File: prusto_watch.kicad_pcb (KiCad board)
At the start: 2 copper layers, 42.2 x 40.9 mm, 55 parts, among them J1 USB_microB_2040002-1, J2 Conn_02x05_Odd_Even, J3 Vibration Motor, J4 Conn_01x06, J5 Conn_01x08, J6 Conn_02x03_Odd_Even, Q3 RUM002N02T2L, SW2 SW_Push, U1 STM32F303RCT6-48, U2 LTC4063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

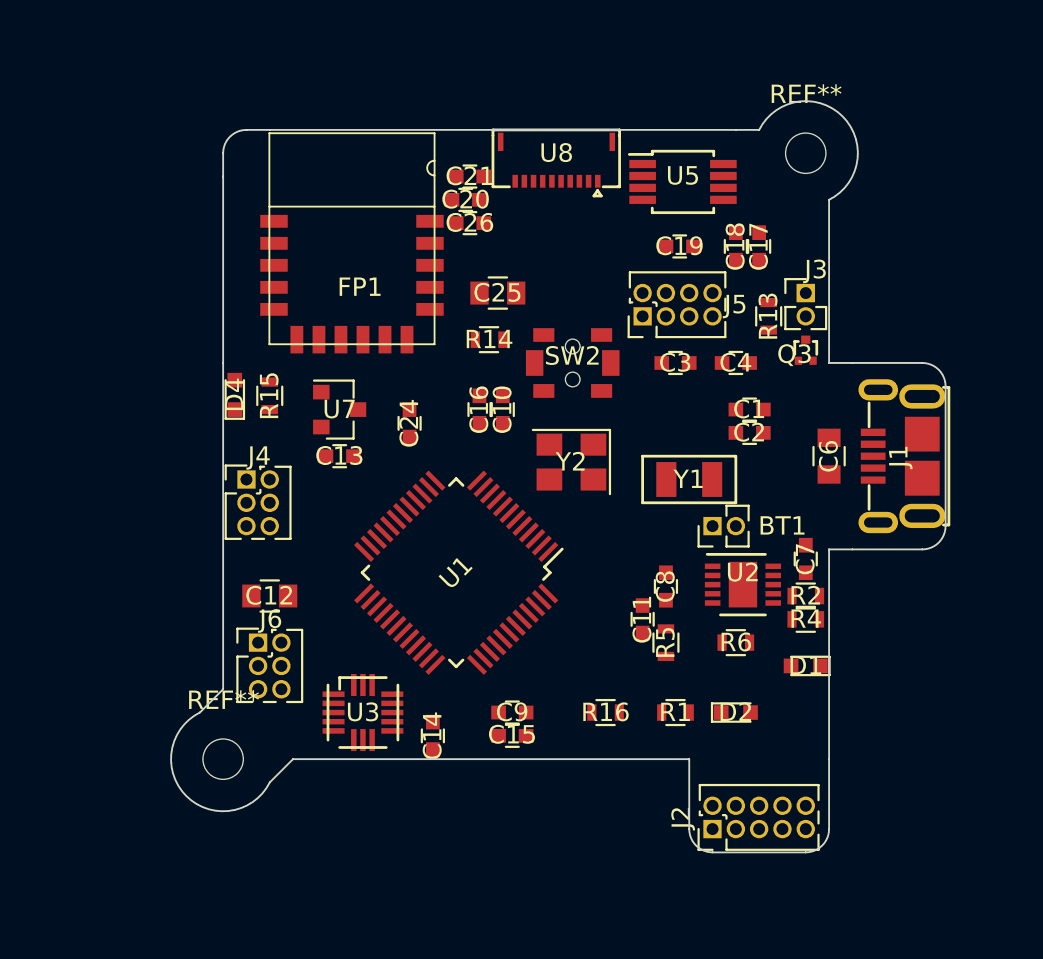
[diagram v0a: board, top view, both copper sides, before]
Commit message: Modify for better positioning
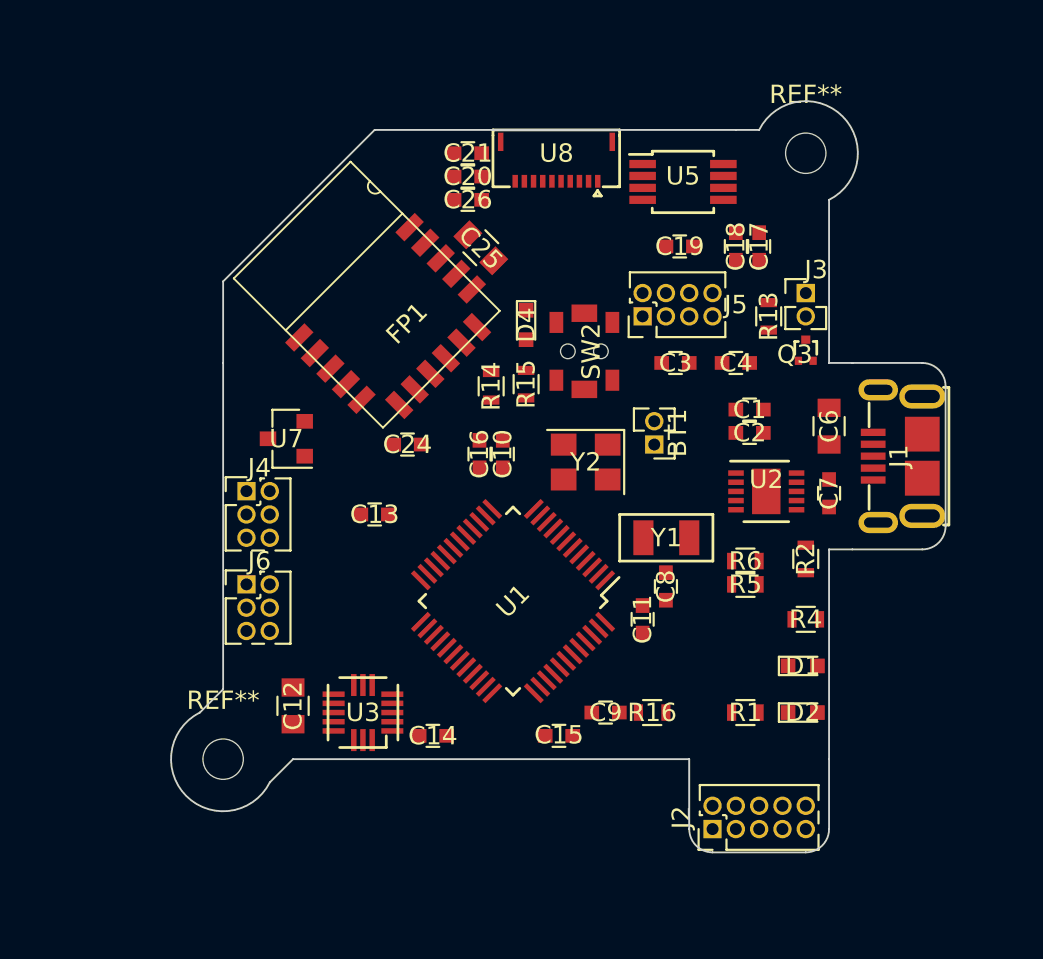
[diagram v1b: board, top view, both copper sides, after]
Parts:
- moved D4 16.3 mm to (146.1, 91.9), turned to 270 degrees
- moved R15 14.0 mm to (146.1, 95.1)
- moved FP1 7.68 mm to (138.3, 97.5), turned to 45 degrees
- moved C12 6.12 mm to (133.3, 112.7), turned to 90 degrees
- moved BT1 5.46 mm to (153.0, 98.4), turned to 180 degrees
- moved R5 5.37 mm to (158.0, 106.0), turned to 180 degrees
- moved U2 5.24 mm to (159.1, 101.0)
- moved C9 5.08 mm to (150.4, 113.0)
- moved R6 4.48 mm to (158.0, 104.8)
- moved R1 3.81 mm to (158.0, 113.0)
- moved C7 3.80 mm to (162.6, 101.1)
- moved C13 3.70 mm to (137.8, 102.2)
- moved D2 3.65 mm to (161.1, 113.0)
- moved U1 3.46 mm to (145.3, 107.0)
- moved Y1 3.41 mm to (153.7, 103.5)
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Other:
- outline, holes or cut-outs redrawn

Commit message: Rework placement
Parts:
- removed REF** (x2): MountingHole_2.2mm_M2, Mounting_Holes:MountingHole_2.2mm_M2
- added J7: Conn_02x03_Counter_Clockwise, Pin_Headers:Pin_Header_Straight_2x03_Pitch1.27mm, F.Cu at (133.3, 111.8)
- added J8: Screw_Terminal_01x01, Mounting_Holes:MountingHole_2.2mm_M2, F.Cu at (127.0, 114.9)
- added J9: Screw_Terminal_01x01, Mounting_Holes:MountingHole_2.2mm_M2, F.Cu at (164.5, 82.5)
- added R3: 10K, Resistors_SMD:R_0603, F.Cu at (138.3, 116.8)
- added R7: 10K, Resistors_SMD:R_0603, F.Cu at (133.9, 116.8)
- added R8: 10K, Resistors_SMD:R_0603, F.Cu at (142.1, 116.8)
- moved J1 39.0 mm to (128.9, 94.6), turned to 270 degrees
- moved J2 36.4 mm to (123.8, 102.9), turned to 0 degrees
- moved D1 29.8 mm to (131.4, 107.5), turned to 270 degrees
- moved C6 29.7 mm to (133.3, 91.8)
- moved J4 29.7 mm to (158.8, 111.1), turned to 180 degrees
- moved C7 28.8 mm to (135.3, 92.0), turned to 90 degrees
- moved R4 27.9 mm to (133.3, 107.4), turned to 90 degrees
- moved C12 26.8 mm to (141.0, 87.0), turned to 0 degrees
- moved R2 26.3 mm to (136.5, 95.9), turned to 0 degrees
- moved C14 24.7 mm to (142.9, 89.7), turned to 270 degrees
- moved R5 24.0 mm to (134.1, 104.1), turned to 0 degrees
- moved R16 23.8 mm to (129.5, 108.7), turned to 90 degrees
- moved U2 23.3 mm to (135.9, 99.1), turned to 90 degrees
- moved U3 23.0 mm to (139.4, 90.2), turned to 0 degrees
- moved BT1 22.5 mm to (130.8, 101.6)
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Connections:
- J1 pad 2: (no net) -> /USB_N
- J1 pad 3: (no net) -> /USB_P
- U1 pad 21: /RX_BLE -> (no net)
- U1 pad 22: /TX_BLE -> (no net)
- U1 pad 32: (no net) -> /USB_N
- U1 pad 33: (no net) -> /USB_P
- U1 pad 42: (no net) -> /RX_BLE
- U1 pad 43: (no net) -> /TX_BLE
- U1 pad 45: (no net) -> /BUTTON1
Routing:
- net /USB_P: track 0.00 -> 0.78 mm
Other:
- board outline removed
- net class Default: trace_width 0.254 -> 0.2032

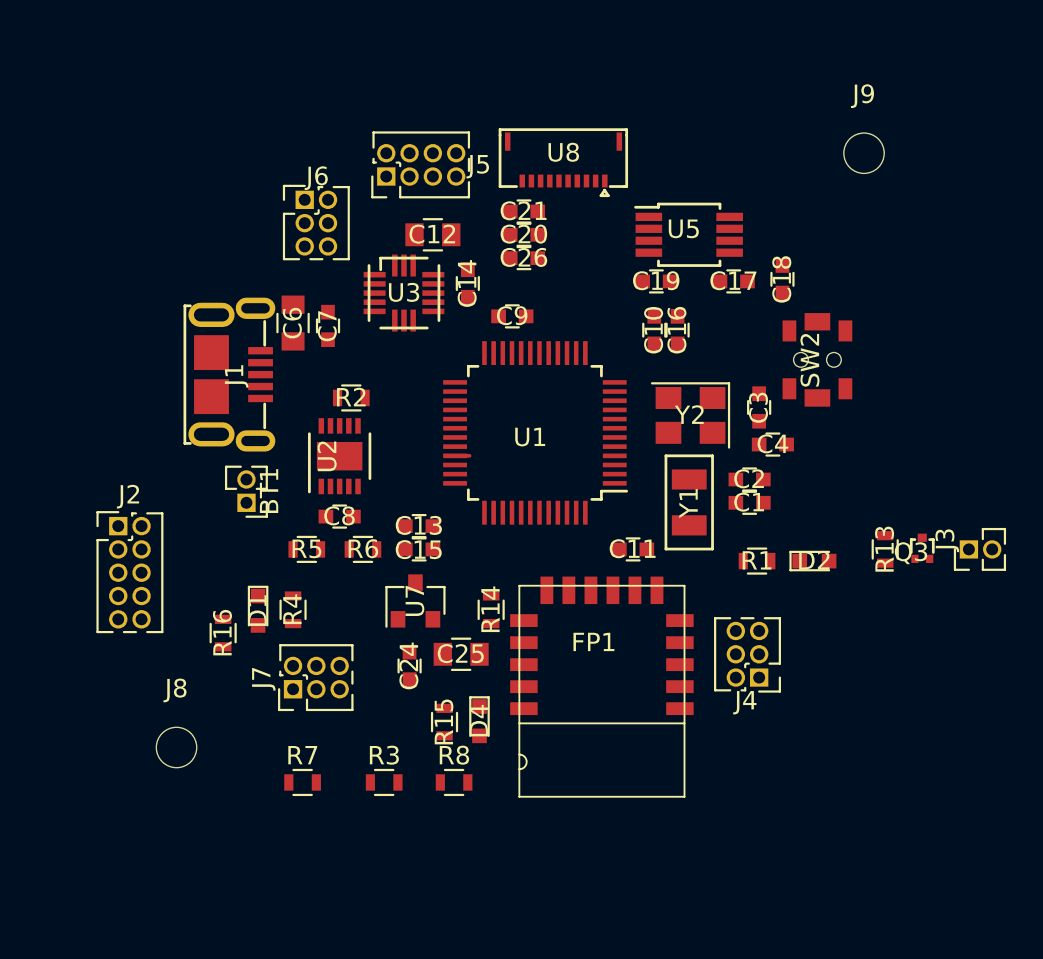
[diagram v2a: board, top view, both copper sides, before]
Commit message: Switch PMIC with USB input
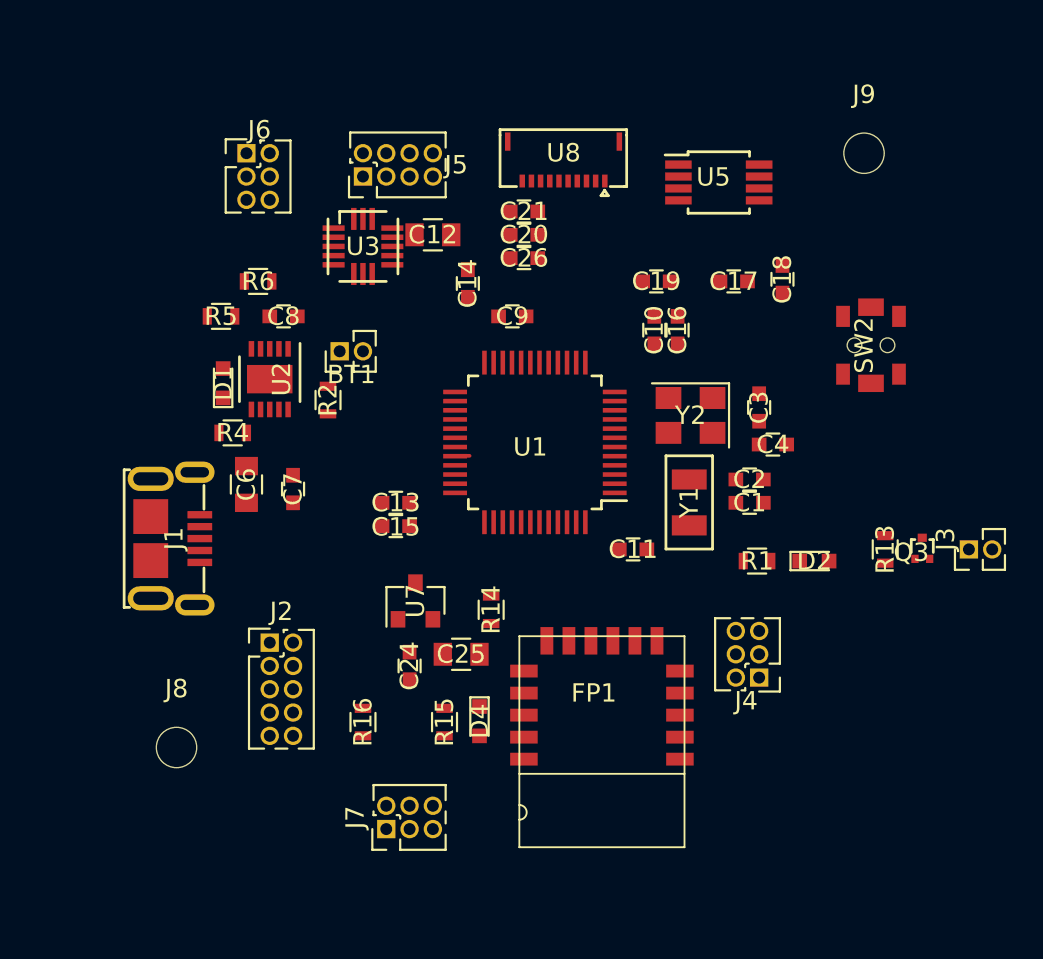
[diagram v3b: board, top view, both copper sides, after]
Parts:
- removed R3, R7, R8: 10K, Resistors_SMD:R_0603
- moved R6 15.7 mm to (131.4, 89.5)
- moved R5 13.5 mm to (129.4, 91.4)
- moved D1 12.5 mm to (129.5, 95.1), turned to 90 degrees
- moved C8 11.3 mm to (132.8, 91.4)
- moved J2 10.4 mm to (132.1, 109.2)
- moved R4 10.2 mm to (130.1, 97.8), turned to 0 degrees
- moved BT1 9.69 mm to (135.9, 93.3), turned to 90 degrees
- moved J1 9.53 mm to (125.6, 103.5)
- moved J7 9.16 mm to (138.4, 119.4)
- moved C6 9.15 mm to (130.8, 100.6)
- moved C7 9.09 mm to (133.3, 100.8)
- moved R16 9.03 mm to (137.2, 113.5)
- moved U2 5.67 mm to (132.1, 94.9), turned to 270 degrees
- moved J6 4.07 mm to (130.8, 82.5)
- moved U3 3.38 mm to (137.2, 87.6)
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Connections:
- J7 pad 4: /BUTTON3 -> (no net)
- J7 pad 5: /BUTTON2 -> (no net)
- U1 pad 19: /BLE_CONF -> (no net)
- U1 pad 20: /BLE_nRST -> (no net)
- U1 pad 40: (no net) -> /BLE_CONF
- U1 pad 41: (no net) -> /BLE_nRST

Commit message: Finalize Routing
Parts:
- J5: value Conn_01x08 -> Conn_01x06; footprint Pin_Headers:Pin_Header_Straight_2x04_Pitch1.27mm -> Pin_Headers:Pin_Header_Straight_2x03_Pitch1.27mm
- moved SW2 37.4 mm to (134.9, 115.4), turned to 270 degrees
- moved J7 25.7 mm to (162.1, 109.2), turned to 180 degrees
- moved J5 19.3 mm to (156.5, 82.8)
- moved J3 15.6 mm to (161.0, 91.4), turned to 0 degrees
- moved J2 12.5 mm to (128.5, 121.2), turned to 90 degrees
- moved J6 11.2 mm to (142.0, 82.3), turned to 270 degrees
- moved Q3 11.1 mm to (160.7, 94.8), turned to 270 degrees
- moved R13 8.20 mm to (160.8, 97.5), turned to 0 degrees
- moved C4 5.11 mm to (157.0, 94.0), turned to 0 degrees
- moved R16 3.42 mm to (134.9, 111.0), turned to 270 degrees
- moved J4 2.95 mm to (157.5, 108.5), turned to 0 degrees
- moved C18 2.89 mm to (160.7, 86.6)
- moved C9 2.66 mm to (142.7, 92.2), turned to 180 degrees
- moved U5 2.32 mm to (155.7, 86.3)
- moved D2 1.89 mm to (160.8, 103.2), turned to 90 degrees
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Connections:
- J4 pad 1: +3V3 -> (no net)
- J4 pad 2: /RX_BLE -> /BLE_nRST
- J4 pad 4: /BLE_CONF -> +3V3
- J4 pad 5: /BLE_nRST -> /RX_BLE
- J5 pad 1: +5V -> /DISP_SCLK
- J5 pad 2: /DISP_EN -> /DISP_SDI
- J5 pad 3: /DISP_SCS -> +5V
- J5 pad 4: /DISP_SDI -> /DISP_SCS
- J5 pad 5: /DISP_SCLK -> /5V_EN
- J5 pad 6: /EXTCOMIN -> GND
- J6 pad 2: /ACC_SCK -> /ACC_CS
- J6 pad 3: /ACC_CS -> GND
- J6 pad 4: /ACC_SDI -> /ACC_SDO
- J6 pad 5: GND -> /ACC_SCK
- J6 pad 6: /ACC_SDO -> /ACC_SDI
- J7 pad 4: (no net) -> /BUTTON1
- J7 pad 5: (no net) -> /LED_1
- J7 pad 6: /BUTTON1 -> /BUTTON2
- U1 pad 11: /5V_EN -> (no net)
- U1 pad 12: /DISP_SCS -> (no net)
- U1 pad 13: /DISP_EN -> /5V_EN
- U1 pad 18: (no net) -> /DISP_SCS
- U1 pad 19: (no net) -> /EXTCOMIN
- U1 pad 20: (no net) -> /DISP_EN
- U1 pad 46: /EXTCOMIN -> /BUTTON2
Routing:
- net +3V3: track 0.00 -> 170.3 mm, vias 0 -> 4
- net GND: track 0.00 -> 83.6 mm, vias 0 -> 34
- net /STM_NRST: track 0.00 -> 35.1 mm, vias 0 -> 6
- net /BLE_nRST: track 0.00 -> 29.9 mm, vias 0 -> 2
- net /TMS: track 0.00 -> 29.6 mm
- net /TDO: track 0.00 -> 27.1 mm, vias 0 -> 2
- net /TCK: track 0.00 -> 26.0 mm
- net /TDI: track 0.00 -> 25.5 mm
- net /ACC_SCK: track 0.00 -> 25.0 mm, vias 0 -> 4
- net +5V: track 0.00 -> 22.7 mm, vias 0 -> 2
- net /ACC_CS: track 0.00 -> 22.5 mm, vias 0 -> 2
- net /DISP_SCS: track 0.00 -> 21.9 mm
- net /LED_1: track 0.00 -> 20.0 mm
- net /DISP_SDI: track 0.00 -> 19.0 mm
- net /ACC_SDI: track 0.00 -> 18.6 mm, vias 0 -> 2
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- added copper zone on B.Cu, net GND
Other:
- board outline added: 43.3 x 43.3 mm

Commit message: Add logos
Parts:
- added REF***: KiCad-Logo2_8mm_SilkScreen, Symbols:KiCad-Logo2_8mm_SilkScreen, B.Cu at (147.3, 108.6)
- added REF***: OSHW-Logo_11.4x12mm_SilkScreen, Symbols:OSHW-Logo_11.4x12mm_SilkScreen, B.Cu at (135.3, 97.8)
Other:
- board text added: "Byron Wasti"
- board text added: "Prusto Watch"
- board text added: "V0.3.0"

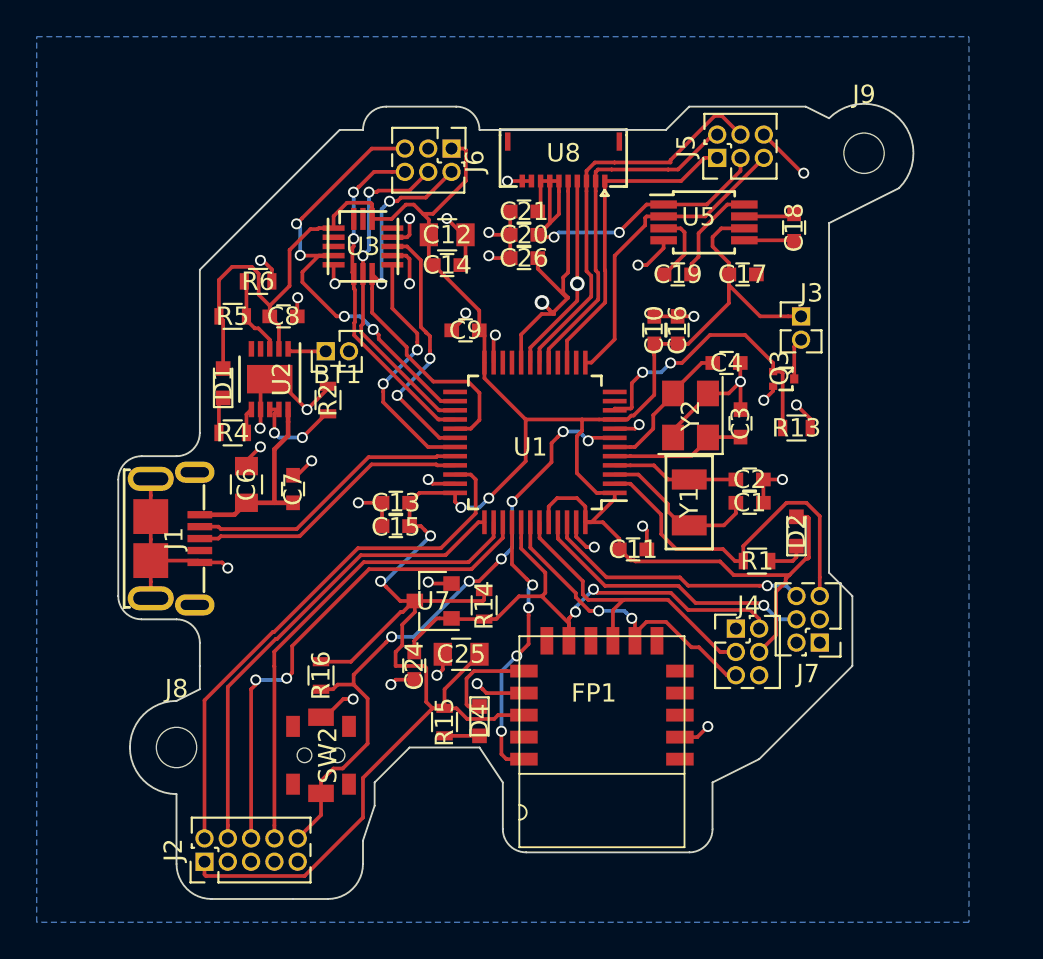
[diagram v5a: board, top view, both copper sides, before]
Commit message: Widen power traces
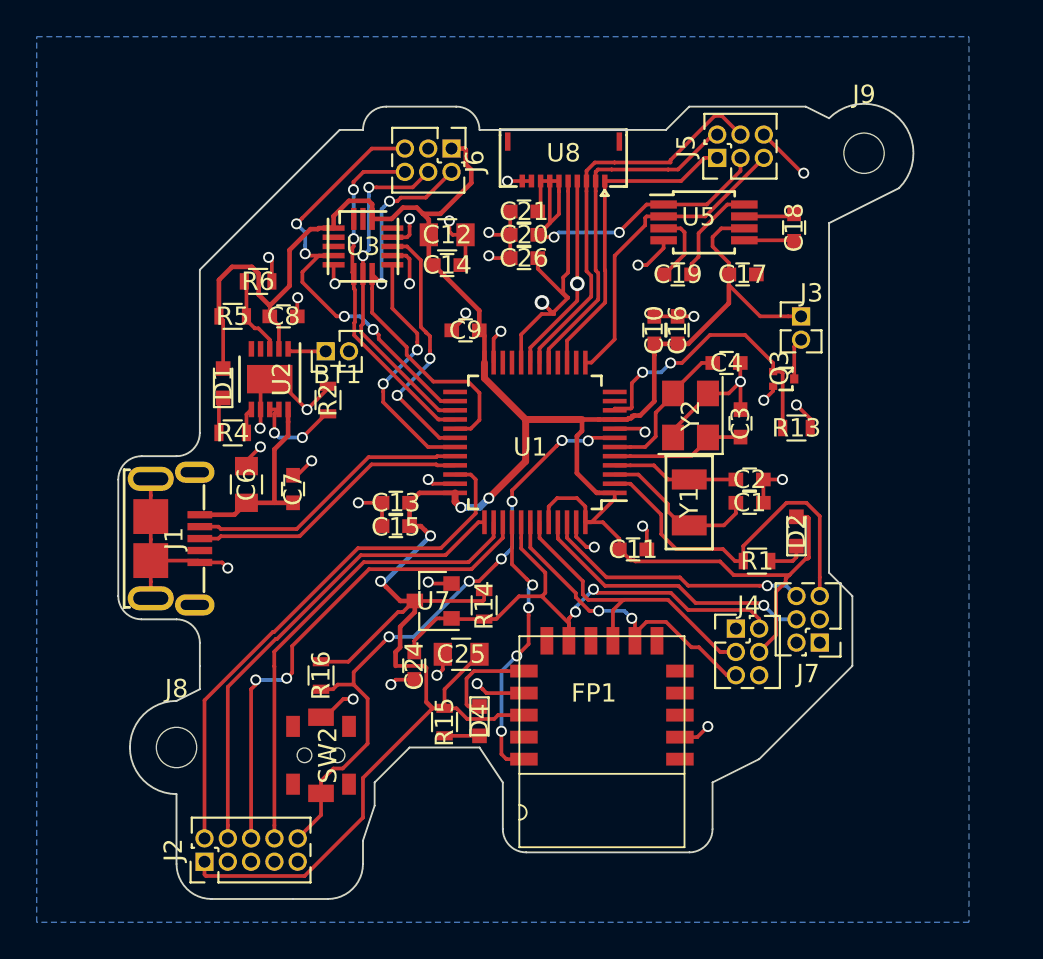
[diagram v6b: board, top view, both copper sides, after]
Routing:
- net +3V3: track 170.3 -> 171.0 mm
- net GND: track 83.6 -> 84.3 mm
- net /STM_NRST: track 35.1 -> 34.5 mm

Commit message: Update schematic and PCB shape
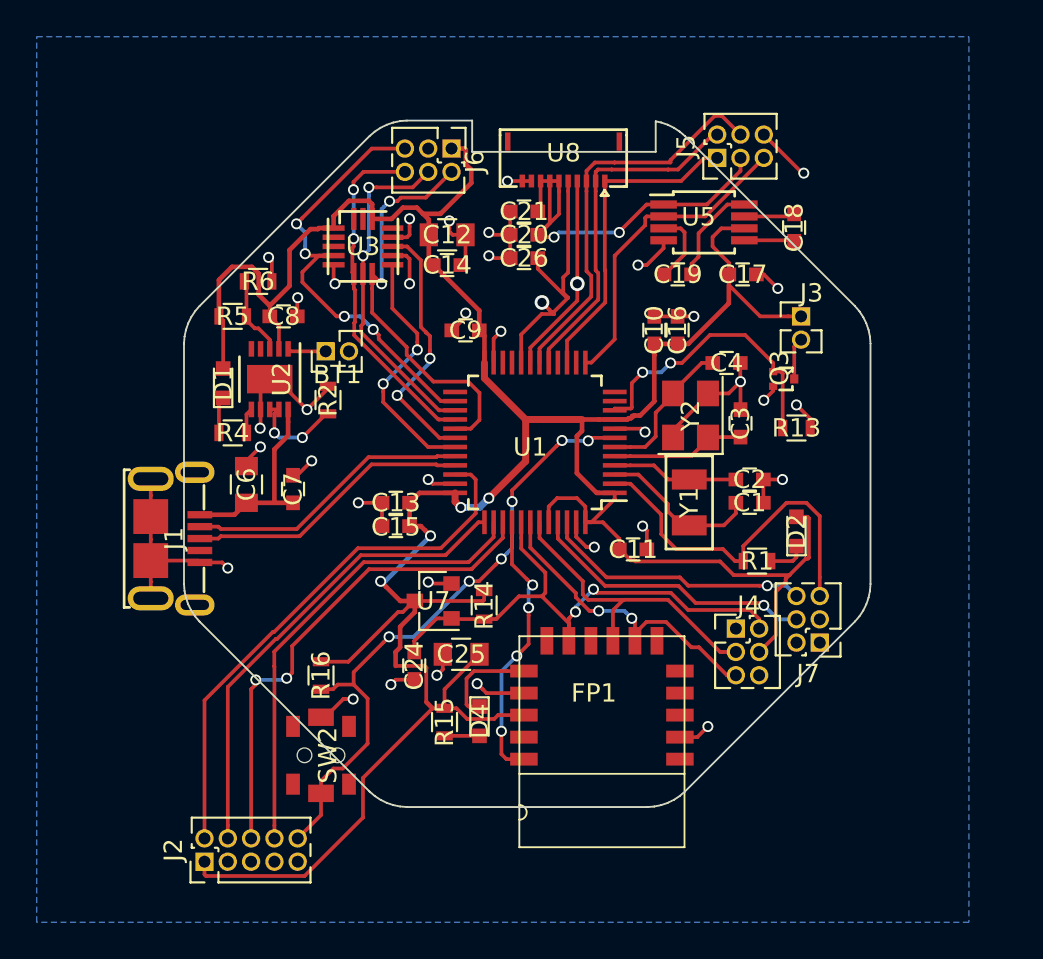
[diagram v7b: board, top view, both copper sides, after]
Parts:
- removed J8, J9: Screw_Terminal_01x01, Mounting_Holes:MountingHole_2.2mm_M2
- removed REF***: KiCad-Logo2_8mm_SilkScreen, Symbols:KiCad-Logo2_8mm_SilkScreen
- removed REF***: OSHW-Logo_11.4x12mm_SilkScreen, Symbols:OSHW-Logo_11.4x12mm_SilkScreen
- R2: value 715 -> 10K
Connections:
- U1 pad 44: +3V3 -> (no net)
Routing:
- net GND: track 84.3 -> 85.8 mm, vias 34 -> 35
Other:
- board size 43.3 x 43.3 mm -> 37.4 x 37.4 mm
- board text removed: "Byron Wasti"
- board text removed: "Prusto Watch"
- board text removed: "V0.3.0"
